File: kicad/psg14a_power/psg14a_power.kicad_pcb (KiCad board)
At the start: 2 copper layers, 81 parts, among them Q1 IRF9Z24N, Q2 IRF9Z24N, Q3 IRF9Z24N, Q4 IRF9Z24N, Q5 IRF9Z24N

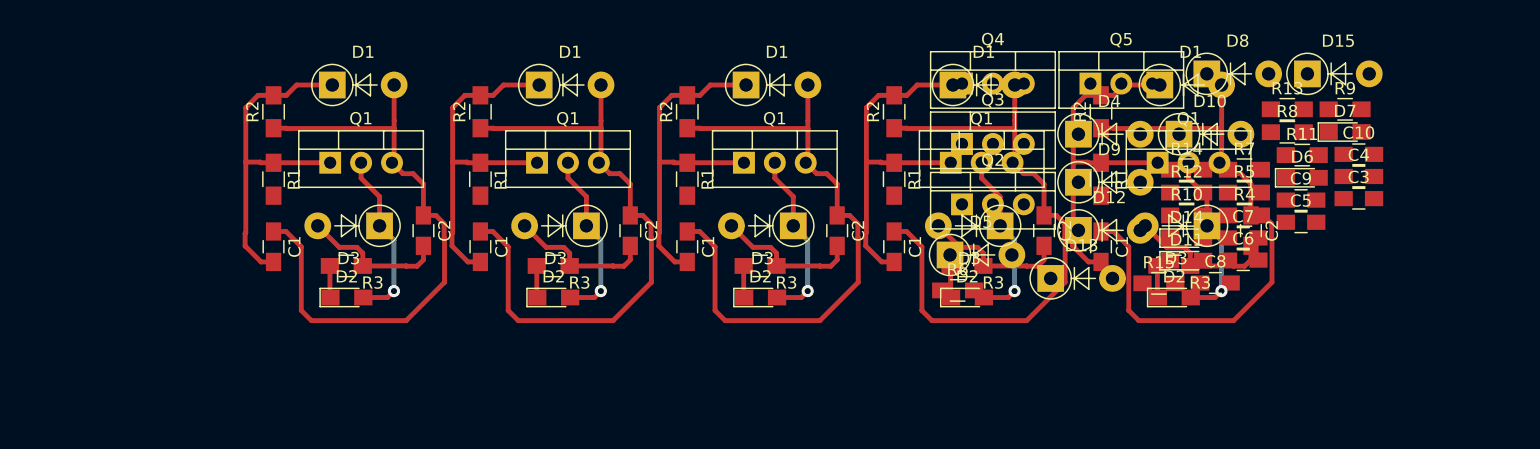
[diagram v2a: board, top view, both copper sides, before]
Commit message: [psg14a_power]New route added
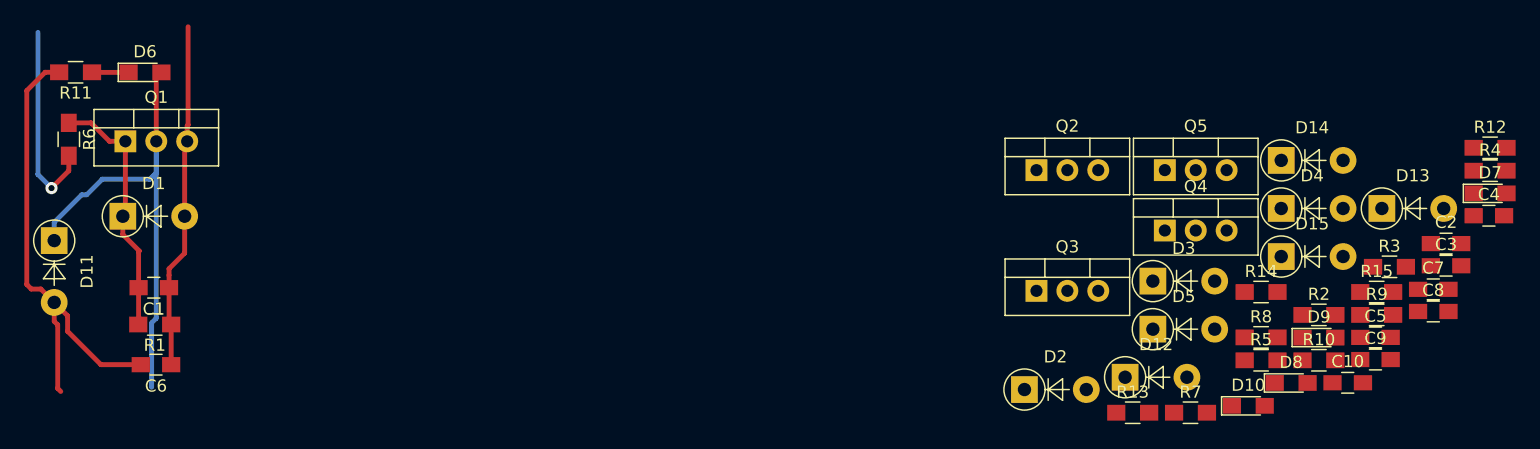
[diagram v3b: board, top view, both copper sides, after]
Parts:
- removed the C1 at (112.2, 46.4)
- removed the C1 at (95.2, 46.4)
- removed the C1 at (78.2, 46.4)
- removed the C1 at (61.2, 46.4)
- removed the C1 at (44.2, 46.4)
- removed the C2 at (124.5, 45.1)
- removed the C2 at (107.5, 45.1)
- removed the C2 at (90.5, 45.1)
- removed the C2 at (73.5, 45.1)
- removed the C2 at (56.5, 45.1)
- removed the D1 at (117.1, 33.2)
- removed the D1 at (100.1, 33.2)
- removed the D1 at (83.1, 33.2)
- removed the D1 at (66.1, 33.2)
- removed the D1 at (49.1, 33.2)
- removed the D2 at (118.3, 50.6)
- removed the D2 at (101.3, 50.6)
- removed the D2 at (84.3, 50.6)
- removed the D2 at (67.3, 50.6)
- removed the D2 at (50.3, 50.6)
- removed the D3 at (120.9, 44.7)
- removed the D3 at (103.9, 44.7)
- removed the D3 at (86.9, 44.7)
- removed the D3 at (69.9, 44.7)
- removed the D3 at (52.9, 44.7)
- removed the Q1 at (116.9, 39.5)
- removed the Q1 at (99.9, 39.5)
- removed the Q1 at (82.9, 39.5)
- removed the Q1 at (65.9, 39.5)
- removed the Q1 at (48.9, 39.5)
- removed the R1 at (112.2, 40.9)
- removed the R1 at (95.2, 40.9)
- removed the R1 at (78.2, 40.9)
- removed the R1 at (61.2, 40.9)
- removed the R1 at (44.2, 40.9)
- removed the R2 at (112.2, 35.4)
- removed the R2 at (95.2, 35.4)
- removed the R2 at (78.2, 35.4)
- removed the R2 at (61.2, 35.4)
- removed the R2 at (44.2, 35.4)
- removed the R3 at (118.2, 48.0)
- removed the R3 at (101.2, 48.0)
- removed the R3 at (84.2, 48.0)
- removed the R3 at (67.2, 48.0)
- removed the R3 at (50.2, 48.0)
- added C1: 10nF, Capacitors_SMD:C_0805_HandSoldering, F.Cu at (34.4, 49.8)
- added C2: 10nF, Capacitors_SMD:C_0805_HandSoldering, F.Cu at (140.6, 46.2)
- added D1: BZX85_C12, Diodes_THT:D_DO-41_SOD81_P5.08mm_Vertical_AnodeUp, F.Cu at (31.8, 43.9)
- added D2: BZX85_C12, Diodes_THT:D_DO-41_SOD81_P5.08mm_Vertical_AnodeUp, F.Cu at (105.9, 58.2)
- added D3: BZX85_C12, Diodes_THT:D_DO-41_SOD81_P5.08mm_Vertical_AnodeUp, F.Cu at (116.5, 49.3)
- added Q1: IRF9Z24N, TO_SOT_Packages_THT:TO-220-3_Vertical, F.Cu at (32.0, 37.8)
- added R1: 10K, Resistors_SMD:R_0805_HandSoldering, F.Cu at (34.5, 52.8)
- added R2: 10K, Resistors_SMD:R_0805_HandSoldering, F.Cu at (130.1, 52.0)
- added R3: 10K, Resistors_SMD:R_0805_HandSoldering, F.Cu at (135.9, 48.1)
- C5: value 1uF 50V -> 10nF
- C7, C9: value 10nF -> 1uF 50V
- D10: value BZX85_C12 -> green; footprint Diodes_THT:D_DO-41_SOD81_P5.08mm_Vertical_AnodeUp -> LEDs:LED_0805_HandSoldering
- D11, D14: value green -> UF4007; footprint LEDs:LED_0805_HandSoldering -> Diodes_THT:D_DO-41_SOD81_P5.08mm_Vertical_AnodeUp
- D13: value BZX85_C12 -> UF4007
- D8, D9: value UF4007 -> green; footprint Diodes_THT:D_DO-41_SOD81_P5.08mm_Vertical_AnodeUp -> LEDs:LED_0805_HandSoldering
- R11, R13, R14: value 10K -> 5k1
- R7, R9: value 5k1 -> 10K
- moved R11 101.0 mm to (28.0, 32.1), turned to 180 degrees
- moved D6 95.5 mm to (33.7, 32.1)
- moved D11 93.1 mm to (26.2, 45.9), turned to 270 degrees
- moved C6 89.8 mm to (34.6, 56.1), turned to 180 degrees
- moved R6 74.1 mm to (27.4, 37.6), turned to 270 degrees
- moved R13 28.0 mm to (114.8, 60.1)
- moved D13 27.8 mm to (135.3, 43.3)
- moved D8 26.3 mm to (127.9, 57.6)
- moved R12 25.2 mm to (144.2, 38.3)
- moved D9 23.5 mm to (130.1, 53.9)
- moved D10 23.0 mm to (124.3, 59.5)
- moved Q4 20.6 mm to (117.5, 45.1)
- moved R4 20.5 mm to (144.2, 40.2)
- moved R7 20.5 mm to (119.6, 60.1)
- moved C10 18.8 mm to (132.5, 57.6)
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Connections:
- C5 pad 2: /gnd -> Net-(C5-Pad2)
- C7 pad 2: Net-(C7-Pad2) -> /gnd
- C9 pad 2: Net-(C9-Pad2) -> /gnd
- D10 pad 1: Net-(C7-Pad2) -> Net-(D10-Pad1)
- D10 pad 2: /+24V -> /Relay_Ctl5
- D11 pad 1: Net-(D11-Pad1) -> /Relay_Ctl1
- D11 pad 2: /Relay_Ctl -> /gnd
- D12 pad 1: /Relay_Ctl -> /Relay_Ctl2
- D13 pad 1: Net-(C9-Pad2) -> /Relay_Ctl3
- D13 pad 2: /+24V -> /gnd
- D14 pad 1: Net-(D14-Pad1) -> /Relay_Ctl4
- D14 pad 2: /Relay_Ctl -> /gnd
- D15 pad 1: /Relay_Ctl -> /Relay_Ctl5
- D15 pad 2: Net-(D15-Pad2) -> /gnd
- D4 pad 1: Net-(C3-Pad2) -> Net-(C4-Pad2)
- D5 pad 1: Net-(C4-Pad2) -> Net-(C5-Pad2)
- D6 pad 2: /Relay_Ctl -> /Relay_Ctl1
- D7 pad 2: /Relay_Ctl -> /Relay_Ctl2
- D8 pad 1: /Relay_Ctl -> Net-(D8-Pad1)
- D8 pad 2: /gnd -> /Relay_Ctl3
- D9 pad 1: /Relay_Ctl -> Net-(D9-Pad1)
- D9 pad 2: /gnd -> /Relay_Ctl4
- Q2 pad 1: Net-(C3-Pad2) -> Net-(C2-Pad2)
- Q2 pad 2: /Relay_Ctl -> /Relay_Ctl2
- Q3 pad 1: Net-(C4-Pad2) -> Net-(C3-Pad2)
- Q3 pad 2: /Relay_Ctl -> /Relay_Ctl3
- Q4 pad 1: Net-(C7-Pad2) -> Net-(C4-Pad2)
- Q4 pad 2: /Relay_Ctl -> /Relay_Ctl4
- Q5 pad 1: Net-(C9-Pad2) -> Net-(C5-Pad2)
- Q5 pad 2: /Relay_Ctl -> /Relay_Ctl5
- R10 pad 1: Net-(C7-Pad2) -> Net-(C5-Pad2)
- R10 pad 2: /In -> /In5
- R11 pad 1: /+24V -> Net-(D6-Pad1)
- R11 pad 2: Net-(C7-Pad2) -> /gnd
- R12 pad 1: Net-(D11-Pad1) -> Net-(D7-Pad1)
- R13 pad 1: Net-(C9-Pad2) -> Net-(D8-Pad1)
- R13 pad 2: /In -> /gnd
- R14 pad 1: /+24V -> Net-(D9-Pad1)
- R14 pad 2: Net-(C9-Pad2) -> /gnd
- R15 pad 1: Net-(D14-Pad1) -> Net-(D10-Pad1)
- R4 pad 1: Net-(C3-Pad2) -> /+24V
- R4 pad 2: /In -> Net-(C4-Pad2)
- R5 pad 1: Net-(C4-Pad2) -> /+24V
- R5 pad 2: /In -> Net-(C5-Pad2)
- R6 pad 1: /+24V -> Net-(C1-Pad2)
- R6 pad 2: Net-(C3-Pad2) -> /In1
- R7 pad 1: Net-(D6-Pad1) -> Net-(C2-Pad2)
- R7 pad 2: /gnd -> /In2
- R8 pad 1: /+24V -> Net-(C3-Pad2)
- R8 pad 2: Net-(C4-Pad2) -> /In3
- R9 pad 1: Net-(D7-Pad1) -> Net-(C4-Pad2)
- R9 pad 2: /gnd -> /In4
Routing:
- net /+24V: track 252.7 -> 28.5 mm
- net Net-(C1-Pad2): track 145.6 -> 21.0 mm
- net /Relay_Ctl: track 72.0 -> 0.00 mm, vias 5 -> 0
- net /Relay_Ctl1: track 0.00 -> 40.4 mm
- net /gnd: track 60.2 -> 39.6 mm
- net /In1: track 0.00 -> 16.5 mm, vias 0 -> 1
- net Net-(D2-Pad1): track 13.1 -> 0.00 mm
- net Net-(D6-Pad1): track 0.00 -> 3.01 mm

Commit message: [psg14a_power] Ready for replication which does not work ;-)
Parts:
- added J1: Power, TerminalBlocks_Phoenix:TerminalBlock_Phoenix_MPT-2.54mm_2pol, F.Cu at (128.1, 71.5)
- added J2: In, TerminalBlocks_Phoenix:TerminalBlock_Phoenix_MPT-2.54mm_6pol, F.Cu at (111.9, 71.5)
- added J3: Out, TerminalBlocks_Phoenix:TerminalBlock_Phoenix_MPT-2.54mm_6pol, F.Cu at (111.9, 78.2)
- C2, C4: value 10nF -> 1uF 50V
- C7, C9: value 1uF 50V -> 10nF
- D10, D7: value green -> BZX85_C12; footprint LEDs:LED_0805_HandSoldering -> Diodes_THT:D_DO-41_SOD81_P5.08mm_Vertical_AnodeUp
- D11, D14: value UF4007 -> green; footprint Diodes_THT:D_DO-41_SOD81_P5.08mm_Vertical_AnodeUp -> LEDs:LED_0805_HandSoldering
- D13: value UF4007 -> BZX85_C12
- D2, D5: value BZX85_C12 -> green; footprint Diodes_THT:D_DO-41_SOD81_P5.08mm_Vertical_AnodeUp -> LEDs:LED_0805_HandSoldering
- D3: value BZX85_C12 -> UF4007
- D6, D9: value green -> UF4007; footprint LEDs:LED_0805_HandSoldering -> Diodes_THT:D_DO-41_SOD81_P5.08mm_Vertical_AnodeUp
- R11, R13, R14: value 5k1 -> 10K
- R3, R6, R9: value 10K -> 5k1
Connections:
- C10 pad 2: /gnd -> /GND
- C2 pad 2: Net-(C2-Pad2) -> /GND
- C4 pad 2: Net-(C4-Pad2) -> /GND
- C6 pad 2: /gnd -> /GND
- C7 pad 2: /gnd -> Net-(C7-Pad2)
- C8 pad 2: /gnd -> /GND
- C9 pad 2: /gnd -> Net-(C9-Pad2)
- D10 pad 1: Net-(D10-Pad1) -> Net-(C7-Pad2)
- D10 pad 2: /Relay_Ctl5 -> /+24V
- D11 pad 1: /Relay_Ctl1 -> Net-(D11-Pad1)
- D11 pad 2: /gnd -> /Out4
- D12 pad 1: /Relay_Ctl2 -> /Out4
- D12 pad 2: /gnd -> /GND
- D13 pad 1: /Relay_Ctl3 -> Net-(C9-Pad2)
- D13 pad 2: /gnd -> /+24V
- D14 pad 1: /Relay_Ctl4 -> Net-(D14-Pad1)
- D14 pad 2: /gnd -> /Out5
- D15 pad 1: /Relay_Ctl5 -> /Out5
- D15 pad 2: /gnd -> /GND
- D2 pad 1: Net-(C2-Pad2) -> Net-(D2-Pad1)
- D2 pad 2: /+24V -> /Out1
- D3 pad 1: Net-(C3-Pad2) -> /Out1
- D3 pad 2: /+24V -> /GND
- D4 pad 1: Net-(C4-Pad2) -> Net-(C3-Pad2)
- D5 pad 1: Net-(C5-Pad2) -> Net-(D5-Pad1)
- D5 pad 2: /+24V -> /Out2
- D6 pad 1: Net-(D6-Pad1) -> /Out2
- D6 pad 2: /Relay_Ctl1 -> /GND
- D7 pad 1: Net-(D7-Pad1) -> Net-(C5-Pad2)
- D7 pad 2: /Relay_Ctl2 -> /+24V
- D8 pad 2: /Relay_Ctl3 -> /Out3
- D9 pad 1: Net-(D9-Pad1) -> /Out3
- D9 pad 2: /Relay_Ctl4 -> /GND
- Q1 pad 2: /Relay_Ctl1 -> /Out1
- Q2 pad 1: Net-(C2-Pad2) -> Net-(C3-Pad2)
- Q2 pad 2: /Relay_Ctl2 -> /Out2
- Q3 pad 1: Net-(C3-Pad2) -> Net-(C5-Pad2)
- Q3 pad 2: /Relay_Ctl3 -> /Out3
- Q4 pad 1: Net-(C4-Pad2) -> Net-(C7-Pad2)
- Q4 pad 2: /Relay_Ctl4 -> /Out4
- Q5 pad 1: Net-(C5-Pad2) -> Net-(C9-Pad2)
- Q5 pad 2: /Relay_Ctl5 -> /Out5
- R1 pad 1: /+24V -> Net-(C1-Pad2)
- R1 pad 2: Net-(C1-Pad2) -> /In1
- R10 pad 1: Net-(C5-Pad2) -> Net-(C7-Pad2)
- R10 pad 2: /In5 -> /In4
- R11 pad 1: Net-(D6-Pad1) -> /+24V
- R11 pad 2: /gnd -> Net-(C7-Pad2)
- R12 pad 1: Net-(D7-Pad1) -> Net-(D11-Pad1)
- R12 pad 2: /gnd -> /GND
- R13 pad 1: Net-(D8-Pad1) -> Net-(C9-Pad2)
- R13 pad 2: /gnd -> /In5
- R14 pad 1: Net-(D9-Pad1) -> /+24V
- R14 pad 2: /gnd -> Net-(C9-Pad2)
- R15 pad 1: Net-(D10-Pad1) -> Net-(D14-Pad1)
- R15 pad 2: /gnd -> /GND
- R2 pad 2: Net-(C2-Pad2) -> Net-(C1-Pad2)
- R3 pad 1: /+24V -> Net-(D2-Pad1)
- R3 pad 2: Net-(C3-Pad2) -> /GND
- R4 pad 1: /+24V -> Net-(C3-Pad2)
- R4 pad 2: Net-(C4-Pad2) -> /In2
- R5 pad 2: Net-(C5-Pad2) -> Net-(C3-Pad2)
- R6 pad 1: Net-(C1-Pad2) -> Net-(D5-Pad1)
- R6 pad 2: /In1 -> /GND
- R7 pad 1: Net-(C2-Pad2) -> Net-(C5-Pad2)
- R7 pad 2: /In2 -> /In3
- R8 pad 1: Net-(C3-Pad2) -> /+24V
- R8 pad 2: /In3 -> Net-(C5-Pad2)
- R9 pad 1: Net-(C4-Pad2) -> Net-(D8-Pad1)
- R9 pad 2: /In4 -> /GND
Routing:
- net /In1: track 16.5 -> 0.00 mm, vias 1 -> 0
- net /GND: track 0.00 -> 16.5 mm, vias 0 -> 1
- net Net-(D6-Pad1): track 3.01 -> 0.00 mm
- net /+24V: track 28.5 -> 31.5 mm

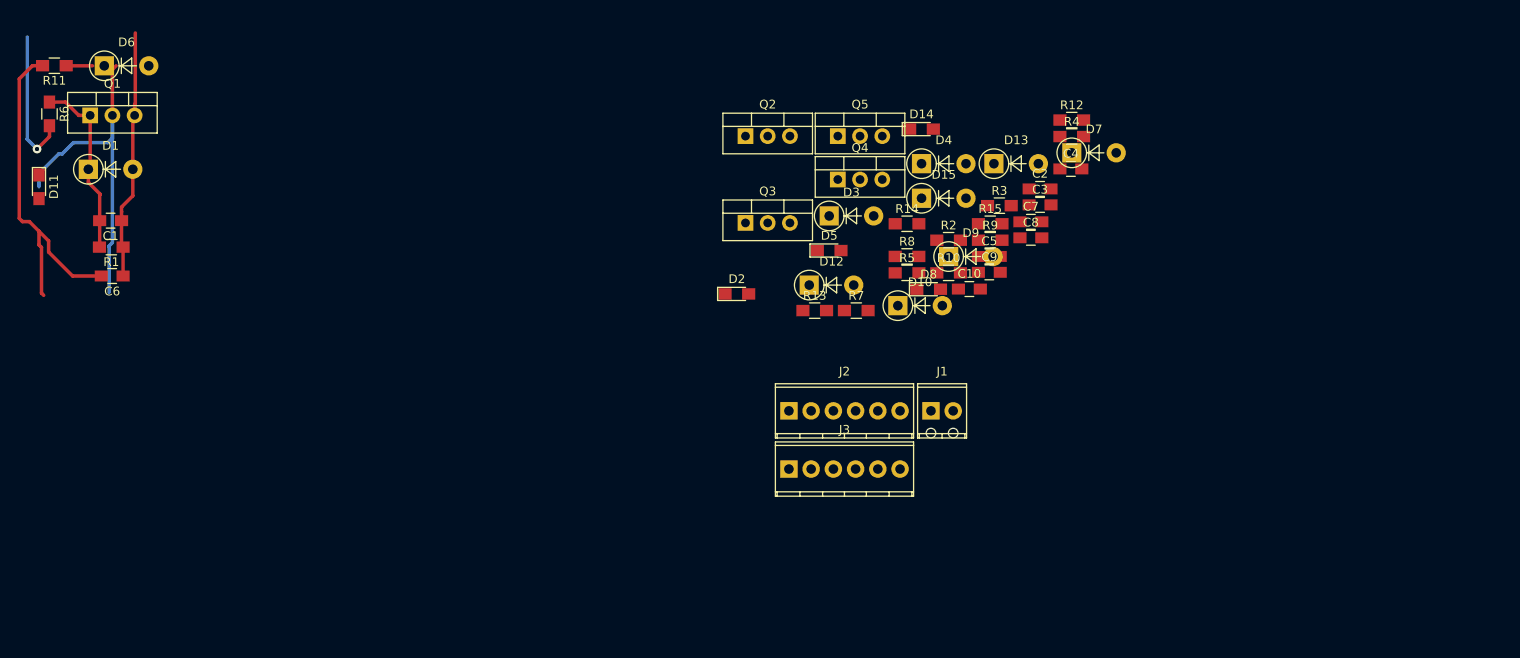
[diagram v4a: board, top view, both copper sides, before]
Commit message: [psg14a_power]New components placement
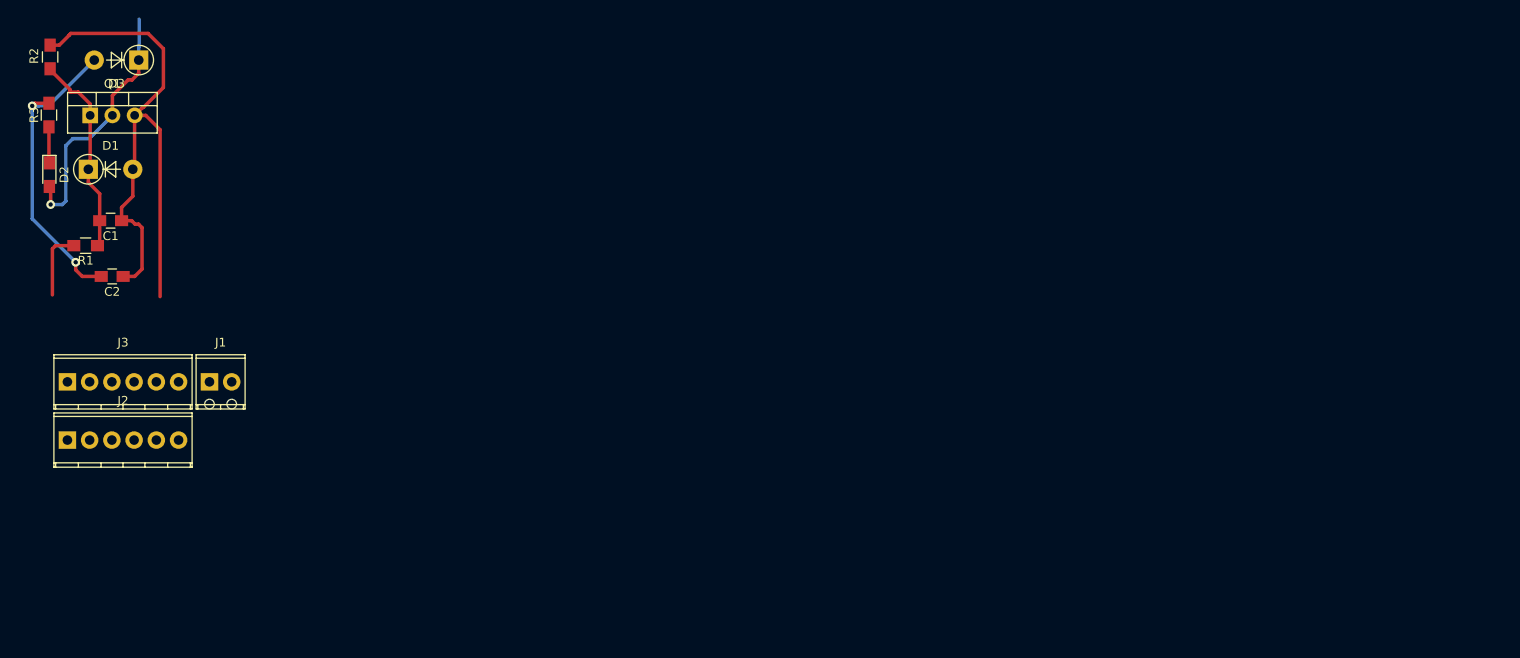
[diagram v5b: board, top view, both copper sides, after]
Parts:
- removed C10, C4, C6, C8: 1uF 50V, Capacitors_SMD:C_0805_HandSoldering
- removed C3, C5, C7, C9: 10nF, Capacitors_SMD:C_0805_HandSoldering
- removed D10, D13, D4, D7: BZX85_C12, Diodes_THT:D_DO-41_SOD81_P5.08mm_Vertical_AnodeUp
- removed D11, D14, D5, D8: green, LEDs:LED_0805_HandSoldering
- removed D12, D15, D6, D9: UF4007, Diodes_THT:D_DO-41_SOD81_P5.08mm_Vertical_AnodeUp
- removed Q2, Q3, Q4, Q5: IRF9Z24N, TO_SOT_Packages_THT:TO-220-3_Vertical
- removed R10, R11, R13, R14, R4, R5, R7, R8: 10K, Resistors_SMD:R_0805_HandSoldering
- removed R12, R15, R6, R9: 5k1, Resistors_SMD:R_0805_HandSoldering
- moved R3 109.1 mm to (27.3, 37.7), turned to 90 degrees
- moved C2 106.5 mm to (34.6, 56.2), turned to 180 degrees
- moved R2 104.8 mm to (27.5, 31.1), turned to 270 degrees
- moved J3 83.0 mm to (29.5, 68.2)
- moved J2 82.5 mm to (29.5, 74.9)
- moved J1 82.5 mm to (45.7, 68.2)
- moved D3 80.9 mm to (37.6, 31.5), turned to 180 degrees
- moved D2 79.7 mm to (27.4, 44.6), turned to 270 degrees
- moved R1 2.94 mm to (31.5, 52.7)
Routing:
- net /Relay_Ctl1: track 40.4 -> 0.00 mm
- net /gnd: track 39.6 -> 0.00 mm
- net /+24V: track 31.5 -> 68.5 mm
- net /Out1: track 0.00 -> 29.7 mm, vias 0 -> 1
- net /GND: track 16.5 -> 35.3 mm, vias 1 -> 2
- net /In1: track 0.00 -> 7.86 mm
- net Net-(D2-Pad1): track 0.00 -> 4.13 mm
- net Net-(C1-Pad2): track 21.0 -> 23.4 mm
